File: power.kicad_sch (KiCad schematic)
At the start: 22 parts, among them J1 USB_C_Receptacle, J2 AVR-ISP-6, J3 Screw_Terminal_01x02, U1 INA226, U2 AMS1117-3.3, U3 ATmega328P-A, Y1 Crystal

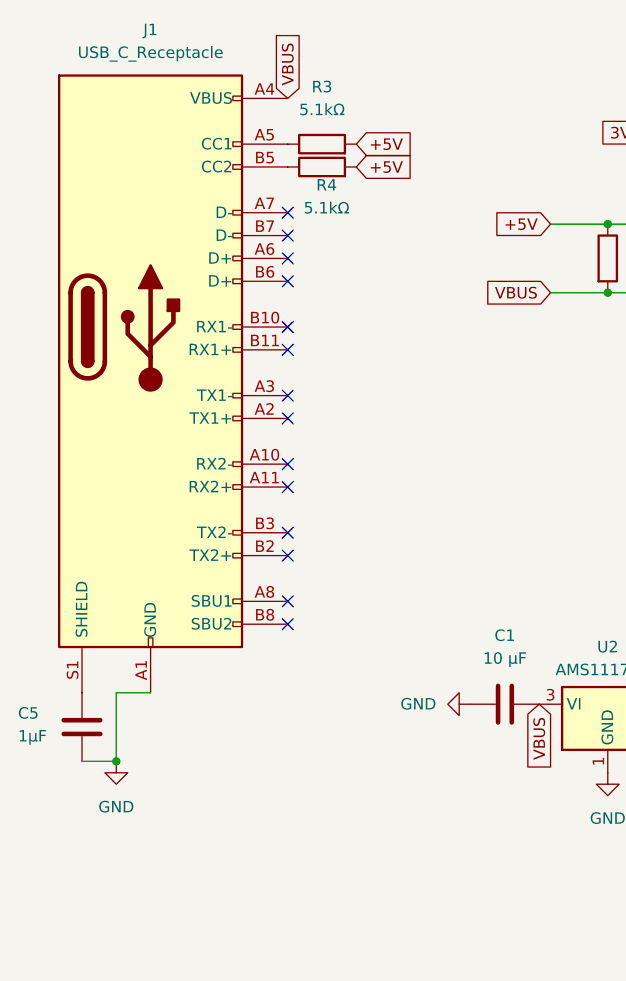
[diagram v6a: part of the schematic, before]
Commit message: Switched USB C out to the proper one
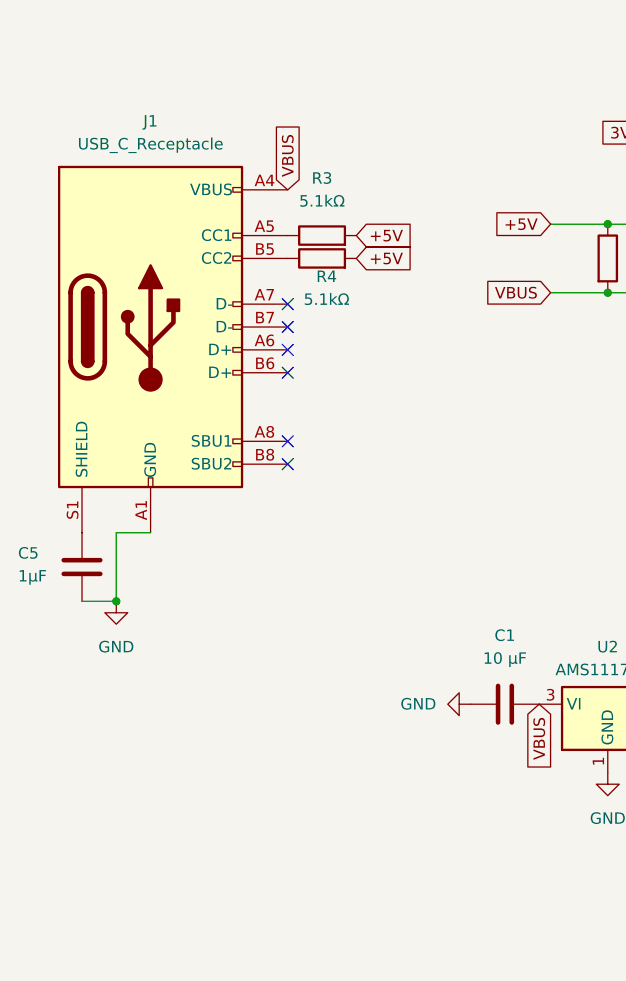
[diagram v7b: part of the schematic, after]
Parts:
- J1: symbol Connector:USB_C_Receptacle -> Connector:USB_C_Receptacle_USB2.0_16P
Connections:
- no-connect marks 21 -> 13
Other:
- moved on the sheet: C5, R3, R4
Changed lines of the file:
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@@
 	)
 	(junction
-		(at 30.48 110.49)
+		(at 30.48 92.71)
 		(diameter 0)
 		(color 0 0 0 0)
@@
 	)
 	(no_connect
-		(at 49.53 85.09)
-	)
-	(no_connect
-		(at 49.53 69.85)
-	)
-	(no_connect
 		(at 125.73 107.95)
 	)
@@
 	)
 	(no_connect
-		(at 49.53 49.53)
+		(at 49.53 67.31)
 	)
 	(no_connect
-		(at 49.53 87.63)
+		(at 49.53 77.47)
 	)
 	(no_connect
@@
 	)
 	(no_connect
-		(at 49.53 80.01)
-	)
-	(no_connect
 		(at 156.21 128.27)
-	)
-	(no_connect
-		(at 49.53 52.07)
-	)
-	(no_connect
-		(at 49.53 92.71)
 	)
 	(no_connect
@@
 	)
 	(no_connect
-		(at 49.53 62.23)
-	)
-	(no_connect
 		(at 156.21 130.81)
 	)
@@
 	)
 	(no_connect
-		(at 49.53 95.25)
+		(at 49.53 74.93)
+	)
+	(no_connect
+		(at 49.53 62.23)
+	)
+	(no_connect
+		(at 49.53 59.69)
 	)
 	(no_connect
 		(at 49.53 64.77)
-	)
-	(no_connect
-		(at 49.53 54.61)
-	)
-	(no_connect
-		(at 49.53 57.15)
-	)
-	(no_connect
-		(at 49.53 72.39)
-	)
-	(no_connect
-		(at 49.53 77.47)
 	)
 	(wire
@@
 	(wire
 		(pts
-			(xy 30.48 102.87) (xy 34.29 102.87)
+			(xy 30.48 85.09) (xy 34.29 85.09)
 		)
 		(stroke
@@
 	(wire
 		(pts
-			(xy 26.67 110.49) (xy 30.48 110.49)
+			(xy 26.67 92.71) (xy 30.48 92.71)
 		)
 		(stroke
@@
 	(wire
 		(pts
-			(xy 30.48 102.87) (xy 30.48 110.49)
+			(xy 30.48 85.09) (xy 30.48 92.71)
 		)
 		(stroke
@@
 	(global_label "+5V"
 		(shape input)
-		(at 57.15 41.91 0)
+		(at 57.15 52.07 0)
 		(fields_autoplaced yes)
 		(effects
@@
 		)
 		(property "Intersheetrefs" "${INTERSHEET_REFS}"
-			(at 63.3515 41.91 0)
+			(at 63.3515 52.07 0)
 			(effects
 				(font
@@
 	(global_label "+5V"
 		(shape input)
-		(at 57.15 44.45 0)
+		(at 57.15 54.61 0)
 		(fields_autoplaced yes)
 		(effects
@@
 		)
 		(property "Intersheetrefs" "${INTERSHEET_REFS}"
-			(at 63.3515 44.45 0)
+			(at 63.3515 54.61 0)
 			(effects
 				(font
@@
 	(global_label "VBUS"
 		(shape input)
-		(at 49.53 36.83 90)
+		(at 49.53 46.99 90)
 		(fields_autoplaced yes)
 		(effects
@@
 		)
 		(property "Intersheetrefs" "${INTERSHEET_REFS}"
-			(at 49.53 29.6004 90)
+			(at 49.53 39.7604 90)
 			(effects
 				(font
@@
 	(symbol
 		(lib_id "power:GND")
-		(at 30.48 110.49 0)
+		(at 30.48 92.71 0)
 		(unit 1)
 		(exclude_from_sim no)
@@
 		(fields_autoplaced yes)
 		(property "Reference" "#PWR03"
-			(at 30.48 116.84 0)
+			(at 30.48 99.06 0)
 			(effects
 				(font
@@
 		)
 		(property "Value" "GND"
-			(at 30.48 115.57 0)
+			(at 30.48 97.79 0)
 			(effects
 				(font
@@
 		)
 		(property "Footprint" ""
-			(at 30.48 110.49 0)
+			(at 30.48 92.71 0)
 			(effects
 				(font
@@
 		)
 		(property "Datasheet" ""
-			(at 30.48 110.49 0)
+			(at 30.48 92.71 0)
 			(effects
 				(font
@@
 		)
 		(property "Description" "Power symbol creates a global label with name \"GND\" , ground"
-			(at 30.48 110.49 0)
+			(at 30.48 92.71 0)
 			(effects
 				(font
@@
 	(symbol
 		(lib_id "Device:R")
-		(at 53.34 41.91 90)
+		(at 53.34 52.07 90)
 		(unit 1)
 		(exclude_from_sim no)
@@
 		(fields_autoplaced yes)
 		(property "Reference" "R3"
-			(at 53.34 35.56 90)
+			(at 53.34 45.72 90)
 			(effects
 				(font
@@
 		)
 		(property "Value" "5.1kΩ"
-			(at 53.34 38.1 90)
+			(at 53.34 48.26 90)
 			(effects
 				(font
@@
 		)
 		(property "Footprint" "Resistor_SMD:R_0603_1608Metric"
-			(at 53.34 43.688 90)
+			(at 53.34 53.848 90)
 			(effects
 				(font
@@
 		)
 		(property "Datasheet" "~"
-			(at 53.34 41.91 0)
+			(at 53.34 52.07 0)
 			(effects
 				(font
@@
 		)
 		(property "Description" "Resistor"
-			(at 53.34 41.91 0)
+			(at 53.34 52.07 0)
 			(effects
 				(font
@@
 	(symbol
 		(lib_id "Device:R")
-		(at 53.34 44.45 90)
+		(at 53.34 54.61 90)
 		(unit 1)
 		(exclude_from_sim no)
@@
 		(dnp no)
 		(property "Reference" "R4"
-			(at 53.848 46.482 90)
+			(at 53.848 56.642 90)
 			(effects
 				(font
@@
 		)
 		(property "Value" "5.1kΩ"
-			(at 53.848 49.022 90)
+			(at 53.848 59.182 90)
 			(effects
 				(font
@@
 		)
 		(property "Footprint" "Resistor_SMD:R_0603_1608Metric"
-			(at 53.34 46.228 90)
+			(at 53.34 56.388 90)
 			(effects
 				(font
@@
 		)
 		(property "Datasheet" "~"
-			(at 53.34 44.45 0)
+			(at 53.34 54.61 0)
 			(effects
 				(font
@@
 		)
 		(property "Description" "Resistor"
-			(at 53.34 44.45 0)
+			(at 53.34 54.61 0)
 			(effects
 				(font
@@
 	(symbol
 		(lib_id "Device:C")
-		(at 26.67 106.68 0)
+		(at 26.67 88.9 0)
 		(unit 1)
 		(exclude_from_sim no)
@@
 		(dnp no)
 		(property "Reference" "C5"
-			(at 19.558 105.156 0)
+			(at 19.558 87.376 0)
 			(effects
 				(font
@@
 		)
 		(property "Value" "1µF"
-			(at 19.558 107.696 0)
+			(at 19.558 89.916 0)
 			(effects
 				(font
@@
 		)
 		(property "Footprint" "Capacitor_SMD:C_0603_1608Metric"
-			(at 27.6352 110.49 0)
+			(at 27.6352 92.71 0)
 			(effects
 				(font
@@
 		)
 		(property "Datasheet" "~"
-			(at 26.67 106.68 0)
+			(at 26.67 88.9 0)
 			(effects
 				(font
@@
 		)
 		(property "Description" "Unpolarized capacitor"
-			(at 26.67 106.68 0)
+			(at 26.67 88.9 0)
 			(effects
 				(font
@@
 	)
 	(symbol
-		(lib_id "Connector:USB_C_Receptacle")
+		(lib_id "Connector:USB_C_Receptacle_USB2.0_16P")
 		(at 34.29 62.23 0)
 		(unit 1)
@@
 		(fields_autoplaced yes)
 		(property "Reference" "J1"
-			(at 34.29 29.21 0)
+			(at 34.29 39.37 0)
 			(effects
 				(font
@@
 		)
 		(property "Value" "USB_C_Receptacle"
-			(at 34.29 31.75 0)
+			(at 34.29 41.91 0)
 			(effects
 				(font
@@
 			)
 		)
-		(property "Description" "USB Full-Featured Type-C Receptacle connector"
+		(property "Description" "USB 2.0-only 16P Type-C Receptacle connector"
 			(at 34.29 62.23 0)
 			(effects
@@
 			)
 		)
-		(pin "A2"
-		)
 		(pin "B12"
 		)
@@
 		(pin "A9"
 		)
-		(pin "B10"
-		)
 		(pin "B8"
 		)
@@
 		(pin "A6"
 		)
-		(pin "B11"
-		)
 		(pin "A12"
 		)
@@
 		(pin "B9"
 		)
-		(pin "A3"
-		)
-		(pin "A10"
-		)
-		(pin "A11"
-		)
-		(pin "B2"
-		)
-		(pin "B3"
-		)
 		(pin "A8"
